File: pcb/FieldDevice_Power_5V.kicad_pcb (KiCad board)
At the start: 2 copper layers, 25 parts, among them J1 Itp_1, J2 V in 6-18V, J3 Itp_2, J4 V out 5V, J5 Vtp_2, J6 Vtp_1, J7 Battery, U1 TPS54232

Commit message: More on the layout
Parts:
- BT1: moved to B.Cu
- D1: value D_Schottky -> B130-13-F
- D2: value D_Schottky -> B130-13-F; footprint Diodes_SMD:D_SOD-123F -> FieldDevice_Power_5V:B130-13-F
- D3: footprint Diodes_SMD:D_SOD-123F -> FieldDevice_Power_5V:D_SOD-123F
- J1, J2, J3, J4, J5, J6: footprint Pin_Headers:Pin_Header_Straight_1x02_Pitch2.54mm -> Pin_Headers:Pin_Header_Angled_1x02_Pitch2.54mm
- J7: footprint Pin_Headers:Pin_Header_Straight_1x01 -> Pin_Headers:Pin_Header_Angled_1x01
- moved J5 98.1 mm to (70.9, 48.5), turned to 90 degrees
- moved D2 94.9 mm to (74.4, 80.1), turned to 270 degrees
- moved D1 94.1 mm to (75.9, 74.9)
- moved C4 90.4 mm to (84.1, 61.7), turned to 270 degrees
- moved J1 88.9 mm to (66.0, 73.4), turned to 180 degrees
- moved C2 88.5 mm to (80.0, 68.7), turned to 90 degrees
- moved J3 88.3 mm to (77.2, 48.5), turned to 90 degrees
- moved C3 86.4 mm to (84.2, 68.6), turned to 90 degrees
- moved R1 85.2 mm to (89.4, 77.0)
- moved C7 77.8 mm to (93.0, 75.4)
- moved L1 75.0 mm to (95.2, 57.4), turned to 180 degrees
- moved C1 72.4 mm to (108.0, 66.8)
- moved R4 72.3 mm to (101.3, 74.4)
- moved U1 72.0 mm to (94.2, 69.8)
- moved BT1 71.8 mm to (90.2, 50.8)
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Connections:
- J6 pad 1: /VIN -> GND
- J6 pad 2: GND -> /VIN
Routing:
- net /Vout: track 0.00 -> 79.2 mm
- net /V+: track 0.00 -> 14.0 mm
- net /VSENSE: track 0.00 -> 13.4 mm
- net /BATT: track 0.00 -> 12.9 mm, vias 0 -> 1
- net /COMP: track 0.00 -> 6.49 mm
- net GND: track 0.00 -> 6.30 mm
- net Net-(C6-Pad1): track 0.00 -> 2.43 mm
- added copper zone on F.Cu, net /PH
- added copper zone on F.Cu, net /VIN
- added copper zone on F.Cu, net /Vout
- added copper zone on B.Cu, net GND
- added copper zone on F.Cu, net GND
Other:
- net class Default: clearance 0.2 -> 0.254; trace_width 0.25 -> 0.254; via_dia 0.6 -> 0.381; via_drill 0.4 -> 0.254
- rule pad_to_mask_clearance: 0.2 -> 0
- rule trace_clearance: 0.2 -> 0.254
- rule trace_min: 0.2 -> 0.254
- rule via_min_drill: 0.3 -> 0.254
- rule via_min_size: 0.4 -> 0.381

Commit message: Finishing up the layout
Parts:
- added ST**: STITCH_VIA, FieldDevice_Power_5V:STITCH_VIA, F.Cu at (95.8, 77.2)
- added ST**: STITCH_VIA, FieldDevice_Power_5V:STITCH_VIA, F.Cu at (94.7, 73.4)
- added ST**: STITCH_VIA, FieldDevice_Power_5V:STITCH_VIA, F.Cu at (93.2, 81.0)
- added ST**: STITCH_VIA, FieldDevice_Power_5V:STITCH_VIA, F.Cu at (90.7, 81.0)
- added ST**: STITCH_VIA, FieldDevice_Power_5V:STITCH_VIA, F.Cu at (88.1, 81.0)
- added ST**: STITCH_VIA, FieldDevice_Power_5V:STITCH_VIA, F.Cu at (85.6, 81.0)
- added ST**: STITCH_VIA, FieldDevice_Power_5V:STITCH_VIA, F.Cu at (83.1, 81.0)
- added ST**: STITCH_VIA, FieldDevice_Power_5V:STITCH_VIA, F.Cu at (80.5, 81.0)
- added ST**: STITCH_VIA, FieldDevice_Power_5V:STITCH_VIA, F.Cu at (78.0, 81.0)
- added ST**: STITCH_VIA, FieldDevice_Power_5V:STITCH_VIA, F.Cu at (72.9, 81.0)
- added ST**: STITCH_VIA, FieldDevice_Power_5V:STITCH_VIA, F.Cu at (70.4, 81.0)
- added ST**: STITCH_VIA, FieldDevice_Power_5V:STITCH_VIA, F.Cu at (67.8, 81.0)
- added ST**: STITCH_VIA, FieldDevice_Power_5V:STITCH_VIA, F.Cu at (94.7, 72.1)
- added ST**: STITCH_VIA, FieldDevice_Power_5V:STITCH_VIA, F.Cu at (65.3, 81.0)
- added ST**: STITCH_VIA, FieldDevice_Power_5V:STITCH_VIA, F.Cu at (88.1, 67.3)
- added ST**: STITCH_VIA, FieldDevice_Power_5V:STITCH_VIA, F.Cu at (78.0, 67.3)
- added ST**: STITCH_VIA, FieldDevice_Power_5V:STITCH_VIA, F.Cu at (75.4, 67.3)
- added ST**: STITCH_VIA, FieldDevice_Power_5V:STITCH_VIA, F.Cu at (70.4, 67.3)
- added ST**: STITCH_VIA, FieldDevice_Power_5V:STITCH_VIA, F.Cu at (65.3, 67.3)
- added ST**: STITCH_VIA, FieldDevice_Power_5V:STITCH_VIA, F.Cu at (88.1, 64.8)
- added ST**: STITCH_VIA, FieldDevice_Power_5V:STITCH_VIA, F.Cu at (85.6, 64.8)
- added ST**: STITCH_VIA, FieldDevice_Power_5V:STITCH_VIA, F.Cu at (83.1, 64.8)
- added ST**: STITCH_VIA, FieldDevice_Power_5V:STITCH_VIA, F.Cu at (80.5, 64.8)
- added ST**: STITCH_VIA, FieldDevice_Power_5V:STITCH_VIA, F.Cu at (94.7, 70.9)
- added ST**: STITCH_VIA, FieldDevice_Power_5V:STITCH_VIA, F.Cu at (78.0, 64.8)
- added ST**: STITCH_VIA, FieldDevice_Power_5V:STITCH_VIA, F.Cu at (75.4, 64.8)
- added ST**: STITCH_VIA, FieldDevice_Power_5V:STITCH_VIA, F.Cu at (72.9, 64.8)
- added ST**: STITCH_VIA, FieldDevice_Power_5V:STITCH_VIA, F.Cu at (70.4, 64.8)
- added ST**: STITCH_VIA, FieldDevice_Power_5V:STITCH_VIA, F.Cu at (65.3, 64.8)
- added ST**: STITCH_VIA, FieldDevice_Power_5V:STITCH_VIA, F.Cu at (93.2, 62.2)
- added ST**: STITCH_VIA, FieldDevice_Power_5V:STITCH_VIA, F.Cu at (90.7, 62.2)
- added ST**: STITCH_VIA, FieldDevice_Power_5V:STITCH_VIA, F.Cu at (88.1, 62.2)
- added ST**: STITCH_VIA, FieldDevice_Power_5V:STITCH_VIA, F.Cu at (85.6, 62.2)
- added ST**: STITCH_VIA, FieldDevice_Power_5V:STITCH_VIA, F.Cu at (83.1, 62.2)
- added ST**: STITCH_VIA, FieldDevice_Power_5V:STITCH_VIA, F.Cu at (94.7, 69.6)
- added ST**: STITCH_VIA, FieldDevice_Power_5V:STITCH_VIA, F.Cu at (80.5, 62.2)
- added ST**: STITCH_VIA, FieldDevice_Power_5V:STITCH_VIA, F.Cu at (78.0, 62.2)
- added ST**: STITCH_VIA, FieldDevice_Power_5V:STITCH_VIA, F.Cu at (75.4, 62.2)
- added ST**: STITCH_VIA, FieldDevice_Power_5V:STITCH_VIA, F.Cu at (72.9, 62.2)
- added ST**: STITCH_VIA, FieldDevice_Power_5V:STITCH_VIA, F.Cu at (70.4, 62.2)
- added ST**: STITCH_VIA, FieldDevice_Power_5V:STITCH_VIA, F.Cu at (67.8, 62.2)
- added ST**: STITCH_VIA, FieldDevice_Power_5V:STITCH_VIA, F.Cu at (65.3, 62.2)
- added ST**: STITCH_VIA, FieldDevice_Power_5V:STITCH_VIA, F.Cu at (93.7, 73.4)
- added ST**: STITCH_VIA, FieldDevice_Power_5V:STITCH_VIA, F.Cu at (93.7, 72.1)
- added ST**: STITCH_VIA, FieldDevice_Power_5V:STITCH_VIA, F.Cu at (93.7, 70.9)
- added ST**: STITCH_VIA, FieldDevice_Power_5V:STITCH_VIA, F.Cu at (93.7, 69.6)
- added ST**: STITCH_VIA, FieldDevice_Power_5V:STITCH_VIA, F.Cu at (94.7, 68.3)
- added ST**: STITCH_VIA, FieldDevice_Power_5V:STITCH_VIA, F.Cu at (93.7, 68.3)
- added ST**: STITCH_VIA, FieldDevice_Power_5V:STITCH_VIA, F.Cu at (94.7, 78.5)
- added ST**: STITCH_VIA, FieldDevice_Power_5V:STITCH_VIA, F.Cu at (113.5, 91.2)
- added ST**: STITCH_VIA, FieldDevice_Power_5V:STITCH_VIA, F.Cu at (111.0, 91.2)
- added ST**: STITCH_VIA, FieldDevice_Power_5V:STITCH_VIA, F.Cu at (108.5, 91.2)
- added ST**: STITCH_VIA, FieldDevice_Power_5V:STITCH_VIA, F.Cu at (105.9, 91.2)
- added ST**: STITCH_VIA, FieldDevice_Power_5V:STITCH_VIA, F.Cu at (103.4, 91.2)
- added ST**: STITCH_VIA, FieldDevice_Power_5V:STITCH_VIA, F.Cu at (100.8, 91.2)
- added ST**: STITCH_VIA, FieldDevice_Power_5V:STITCH_VIA, F.Cu at (98.3, 91.2)
- added ST**: STITCH_VIA, FieldDevice_Power_5V:STITCH_VIA, F.Cu at (95.8, 91.2)
- added ST**: STITCH_VIA, FieldDevice_Power_5V:STITCH_VIA, F.Cu at (93.2, 91.2)
- added ST**: STITCH_VIA, FieldDevice_Power_5V:STITCH_VIA, F.Cu at (90.7, 91.2)
- added ST**: STITCH_VIA, FieldDevice_Power_5V:STITCH_VIA, F.Cu at (96.8, 78.5)
- added ST**: STITCH_VIA, FieldDevice_Power_5V:STITCH_VIA, F.Cu at (88.1, 91.2)
- added ST**: STITCH_VIA, FieldDevice_Power_5V:STITCH_VIA, F.Cu at (85.6, 91.2)
- added ST**: STITCH_VIA, FieldDevice_Power_5V:STITCH_VIA, F.Cu at (83.1, 91.2)
- added ST**: STITCH_VIA, FieldDevice_Power_5V:STITCH_VIA, F.Cu at (80.5, 91.2)
- added ST**: STITCH_VIA, FieldDevice_Power_5V:STITCH_VIA, F.Cu at (78.0, 91.2)
- added ST**: STITCH_VIA, FieldDevice_Power_5V:STITCH_VIA, F.Cu at (75.4, 91.2)
- added ST**: STITCH_VIA, FieldDevice_Power_5V:STITCH_VIA, F.Cu at (72.9, 91.2)
- added ST**: STITCH_VIA, FieldDevice_Power_5V:STITCH_VIA, F.Cu at (70.4, 91.2)
- added ST**: STITCH_VIA, FieldDevice_Power_5V:STITCH_VIA, F.Cu at (67.8, 91.2)
- added ST**: STITCH_VIA, FieldDevice_Power_5V:STITCH_VIA, F.Cu at (65.3, 91.2)
- added ST**: STITCH_VIA, FieldDevice_Power_5V:STITCH_VIA, F.Cu at (96.8, 75.9)
- added ST**: STITCH_VIA, FieldDevice_Power_5V:STITCH_VIA, F.Cu at (113.5, 88.6)
- added ST**: STITCH_VIA, FieldDevice_Power_5V:STITCH_VIA, F.Cu at (111.0, 88.6)
- added ST**: STITCH_VIA, FieldDevice_Power_5V:STITCH_VIA, F.Cu at (108.5, 88.6)
- added ST**: STITCH_VIA, FieldDevice_Power_5V:STITCH_VIA, F.Cu at (105.9, 88.6)
- added ST**: STITCH_VIA, FieldDevice_Power_5V:STITCH_VIA, F.Cu at (103.4, 88.6)
- added ST**: STITCH_VIA, FieldDevice_Power_5V:STITCH_VIA, F.Cu at (100.8, 88.6)
- added ST**: STITCH_VIA, FieldDevice_Power_5V:STITCH_VIA, F.Cu at (98.3, 88.6)
- added ST**: STITCH_VIA, FieldDevice_Power_5V:STITCH_VIA, F.Cu at (95.8, 88.6)
- added ST**: STITCH_VIA, FieldDevice_Power_5V:STITCH_VIA, F.Cu at (93.2, 88.6)
- added ST**: STITCH_VIA, FieldDevice_Power_5V:STITCH_VIA, F.Cu at (90.7, 88.6)
- added ST**: STITCH_VIA, FieldDevice_Power_5V:STITCH_VIA, F.Cu at (94.7, 75.9)
- added ST**: STITCH_VIA, FieldDevice_Power_5V:STITCH_VIA, F.Cu at (88.1, 88.6)
- added ST**: STITCH_VIA, FieldDevice_Power_5V:STITCH_VIA, F.Cu at (85.6, 88.6)
- added ST**: STITCH_VIA, FieldDevice_Power_5V:STITCH_VIA, F.Cu at (83.1, 88.6)
- added ST**: STITCH_VIA, FieldDevice_Power_5V:STITCH_VIA, F.Cu at (80.5, 88.6)
- added ST**: STITCH_VIA, FieldDevice_Power_5V:STITCH_VIA, F.Cu at (78.0, 88.6)
- added ST**: STITCH_VIA, FieldDevice_Power_5V:STITCH_VIA, F.Cu at (75.4, 88.6)
- added ST**: STITCH_VIA, FieldDevice_Power_5V:STITCH_VIA, F.Cu at (72.9, 88.6)
- added ST**: STITCH_VIA, FieldDevice_Power_5V:STITCH_VIA, F.Cu at (70.4, 88.6)
- added ST**: STITCH_VIA, FieldDevice_Power_5V:STITCH_VIA, F.Cu at (65.3, 88.6)
- added ST**: STITCH_VIA, FieldDevice_Power_5V:STITCH_VIA, F.Cu at (113.5, 86.1)
- added ST**: STITCH_VIA, FieldDevice_Power_5V:STITCH_VIA, F.Cu at (94.7, 67.1)
- added ST**: STITCH_VIA, FieldDevice_Power_5V:STITCH_VIA, F.Cu at (111.0, 86.1)
- added ST**: STITCH_VIA, FieldDevice_Power_5V:STITCH_VIA, F.Cu at (108.5, 86.1)
- added ST**: STITCH_VIA, FieldDevice_Power_5V:STITCH_VIA, F.Cu at (105.9, 86.1)
- added ST**: STITCH_VIA, FieldDevice_Power_5V:STITCH_VIA, F.Cu at (103.4, 86.1)
- added ST**: STITCH_VIA, FieldDevice_Power_5V:STITCH_VIA, F.Cu at (100.8, 86.1)
- added ST**: STITCH_VIA, FieldDevice_Power_5V:STITCH_VIA, F.Cu at (98.3, 86.1)
- added ST**: STITCH_VIA, FieldDevice_Power_5V:STITCH_VIA, F.Cu at (95.8, 86.1)
- added ST**: STITCH_VIA, FieldDevice_Power_5V:STITCH_VIA, F.Cu at (93.2, 86.1)
- added ST**: STITCH_VIA, FieldDevice_Power_5V:STITCH_VIA, F.Cu at (85.6, 86.1)
- added ST**: STITCH_VIA, FieldDevice_Power_5V:STITCH_VIA, F.Cu at (83.1, 86.1)
- added ST**: STITCH_VIA, FieldDevice_Power_5V:STITCH_VIA, F.Cu at (93.7, 67.1)
- added ST**: STITCH_VIA, FieldDevice_Power_5V:STITCH_VIA, F.Cu at (80.5, 86.1)
- added ST**: STITCH_VIA, FieldDevice_Power_5V:STITCH_VIA, F.Cu at (78.0, 86.1)
- added ST**: STITCH_VIA, FieldDevice_Power_5V:STITCH_VIA, F.Cu at (75.4, 86.1)
- added ST**: STITCH_VIA, FieldDevice_Power_5V:STITCH_VIA, F.Cu at (65.3, 86.1)
- added ST**: STITCH_VIA, FieldDevice_Power_5V:STITCH_VIA, F.Cu at (113.5, 83.6)
- added ST**: STITCH_VIA, FieldDevice_Power_5V:STITCH_VIA, F.Cu at (111.0, 83.6)
- added ST**: STITCH_VIA, FieldDevice_Power_5V:STITCH_VIA, F.Cu at (108.5, 83.6)
- added ST**: STITCH_VIA, FieldDevice_Power_5V:STITCH_VIA, F.Cu at (105.9, 83.6)
- added ST**: STITCH_VIA, FieldDevice_Power_5V:STITCH_VIA, F.Cu at (103.4, 83.6)
- added ST**: STITCH_VIA, FieldDevice_Power_5V:STITCH_VIA, F.Cu at (100.8, 83.6)
- added ST**: STITCH_VIA, FieldDevice_Power_5V:STITCH_VIA, F.Cu at (96.8, 73.4)
- added ST**: STITCH_VIA, FieldDevice_Power_5V:STITCH_VIA, F.Cu at (98.3, 83.6)
- added ST**: STITCH_VIA, FieldDevice_Power_5V:STITCH_VIA, F.Cu at (95.8, 83.6)
- added ST**: STITCH_VIA, FieldDevice_Power_5V:STITCH_VIA, F.Cu at (93.2, 83.6)
- added ST**: STITCH_VIA, FieldDevice_Power_5V:STITCH_VIA, F.Cu at (88.1, 83.6)
- added ST**: STITCH_VIA, FieldDevice_Power_5V:STITCH_VIA, F.Cu at (85.6, 83.6)
- added ST**: STITCH_VIA, FieldDevice_Power_5V:STITCH_VIA, F.Cu at (83.1, 83.6)
- added ST**: STITCH_VIA, FieldDevice_Power_5V:STITCH_VIA, F.Cu at (80.5, 83.6)
- added ST**: STITCH_VIA, FieldDevice_Power_5V:STITCH_VIA, F.Cu at (78.0, 83.6)
- added ST**: STITCH_VIA, FieldDevice_Power_5V:STITCH_VIA, F.Cu at (75.4, 83.6)
- added ST**: STITCH_VIA, FieldDevice_Power_5V:STITCH_VIA, F.Cu at (72.9, 83.6)
- added ST**: STITCH_VIA, FieldDevice_Power_5V:STITCH_VIA, F.Cu at (95.8, 73.4)
- added ST**: STITCH_VIA, FieldDevice_Power_5V:STITCH_VIA, F.Cu at (70.4, 83.6)
- added ST**: STITCH_VIA, FieldDevice_Power_5V:STITCH_VIA, F.Cu at (67.8, 83.6)
- added ST**: STITCH_VIA, FieldDevice_Power_5V:STITCH_VIA, F.Cu at (65.3, 83.6)
- added ST**: STITCH_VIA, FieldDevice_Power_5V:STITCH_VIA, F.Cu at (113.5, 81.0)
- added ST**: STITCH_VIA, FieldDevice_Power_5V:STITCH_VIA, F.Cu at (111.0, 81.0)
- added ST**: STITCH_VIA, FieldDevice_Power_5V:STITCH_VIA, F.Cu at (108.5, 81.0)
- added ST**: STITCH_VIA, FieldDevice_Power_5V:STITCH_VIA, F.Cu at (105.9, 81.0)
- added ST**: STITCH_VIA, FieldDevice_Power_5V:STITCH_VIA, F.Cu at (103.4, 81.0)
- added ST**: STITCH_VIA, FieldDevice_Power_5V:STITCH_VIA, F.Cu at (98.3, 81.0)
- added ST**: STITCH_VIA, FieldDevice_Power_5V:STITCH_VIA, F.Cu at (95.8, 81.0)
- J1, J3, J5, J6: footprint Pin_Headers:Pin_Header_Angled_1x02_Pitch2.54mm -> Pin_Headers:Pin_Header_Straight_1x02_Pitch2.54mm
- J7: footprint Pin_Headers:Pin_Header_Angled_1x01 -> FieldDevice_Power_5V:Pin_Header_Angled_1x01
- moved J2 7.58 mm to (68.1, 66.0)
- moved J7 6.67 mm to (68.1, 89.4)
- moved J1 1.78 mm to (66.0, 71.6), turned to 0 degrees
- moved C1 1.02 mm to (108.0, 67.8)
- moved C2 0.78 mm to (80.8, 68.6)
- moved J4 0.25 mm to (83.6, 48.3)
- moved C3 0.16 mm to (84.3, 68.6)
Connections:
- net Net-(J3-Pad2) renamed /V5+
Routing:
- net /BOOT: track 0.00 -> 28.8 mm, vias 0 -> 2
- net Net-(D1-Pad2): track 0.00 -> 14.4 mm, vias 0 -> 1
- net /EN: track 0.00 -> 10.6 mm
- net /V5+: track 0.00 -> 3.92 mm
- net /SS: track 0.00 -> 3.82 mm
- net /VIN: track 0.00 -> 2.79 mm
- net /V+: track 14.0 -> 14.2 mm, vias 0 -> 1
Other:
- board outline added: 51.6 x 48 mm

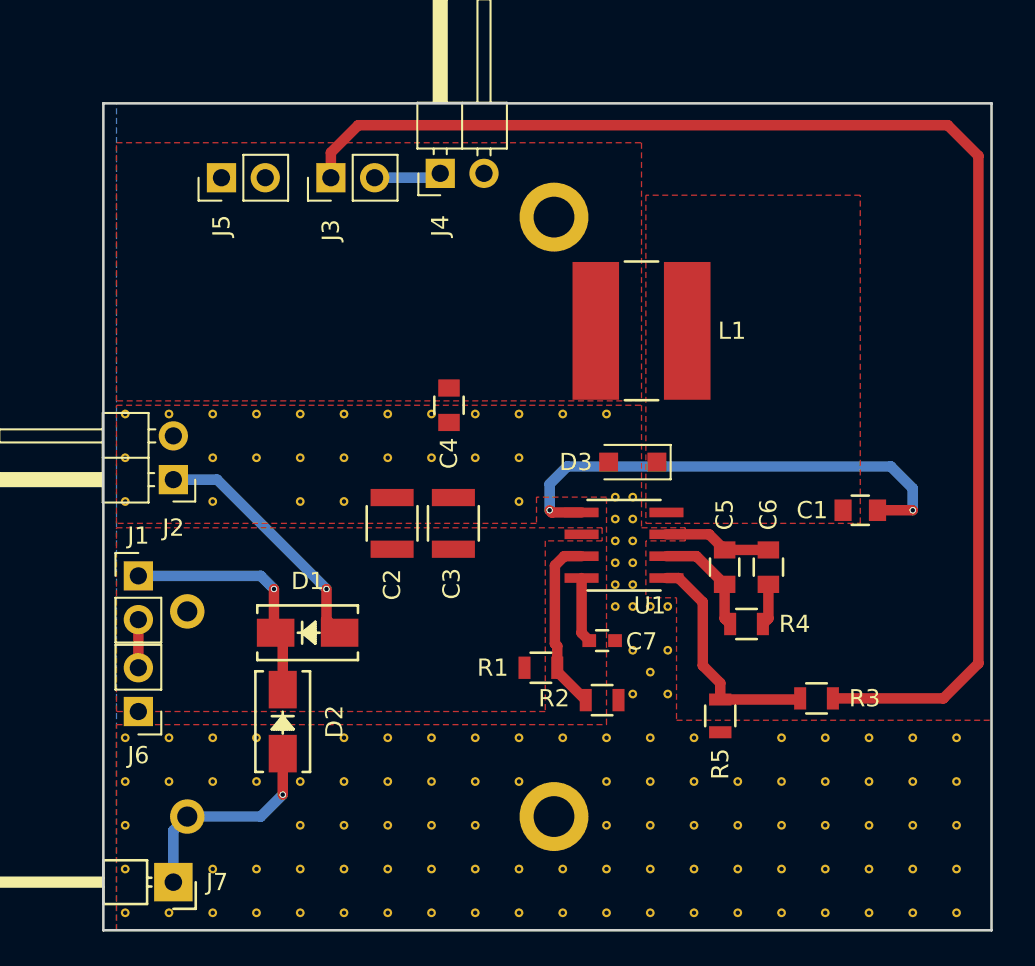
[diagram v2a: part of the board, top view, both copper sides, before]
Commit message: Finalised the layout and prepared Gerbers
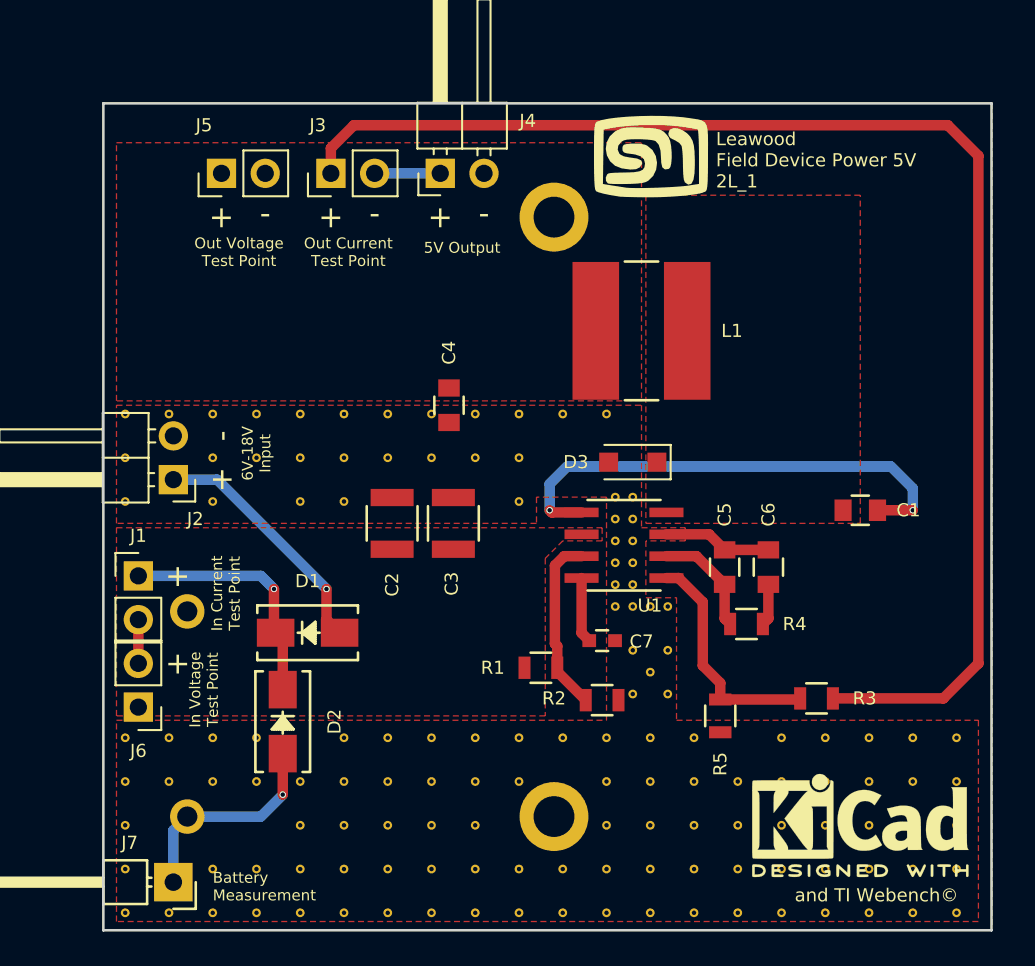
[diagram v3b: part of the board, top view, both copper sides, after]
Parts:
- added G***: LOGO, FieldDevice_Power_5V:MyBasic_rounded_50_1, F.Cu at (95.8, 47.2)
- added REF***: KiCad-Logo2_6mm_SilkScreen, Symbols:KiCad-Logo2_6mm_SilkScreen, F.Cu at (108.0, 86.1)
- moved J3 0.25 mm to (77.2, 48.3)
- moved J5 0.25 mm to (70.9, 48.3)
- moved J6 0.25 mm to (66.0, 79.2)
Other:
- board text added: "+"
- board text added: "-"
- board text added: "5V Output"
- board text added: "6V-18V Input"
- board text added: "Battery Measurement"
- board text added: "In Current Test Point"
- board text added: "In Voltage Test Point"
- board text added: "Leawood Field Device Power 5V 2L_1"
- board text added: "Out Current Test Point"
- board text added: "Out Voltage Test Point"
- board text added: "and TI Webench©"

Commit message: Fixed up some nomenclature
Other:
- board text added: "*"
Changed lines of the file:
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@@
     (area 57.142999 37.430999 120.430191 93.8631)
     (thickness 1.6)
-    (drawings 23)
+    (drawings 24)
     (tracks 68)
     (zones 0)
@@
   )
   (setup
-    (last_trace_width 0.6096)
+    (last_trace_width 0.254)
     (user_trace_width 0.3048)
     (user_trace_width 0.6096)
@@
     (pad_to_mask_clearance 0)
     (aux_axis_origin 0 0)
-    (visible_elements FFFEFF7F)
+    (visible_elements 7FFEEF7F)
     (pcbplotparams
       (layerselection 0x010f8_80000001)
@@
       (drillshape 0)
       (scaleselection 1)
-      (outputdirectory gerbers/))
+      (outputdirectory ../doc/))
   )
   (net 0 "")
@@
     (tags "capacitor 0805")
     (attr smd)
-    (fp_text reference C1 (at 2.794 0) (layer F.SilkS)
+    (fp_text reference C1 (at -0.05 1.682) (layer F.SilkS)
       (effects (font (size 0.762 0.762) (thickness 0.127)))
     )
@@
     (tags "capacitor 1210")
     (attr smd)
-    (fp_text reference C2 (at -3.556 0 90) (layer F.SilkS)
+    (fp_text reference C2 (at 0.08 -2.372 90) (layer F.SilkS)
       (effects (font (size 0.762 0.762) (thickness 0.127)))
     )
@@
     (tags "capacitor 1210")
     (attr smd)
-    (fp_text reference C3 (at -3.5052 -0.1016 90) (layer F.SilkS)
+    (fp_text reference C3 (at -0.02 2.472 90) (layer F.SilkS)
       (effects (font (size 0.762 0.762) (thickness 0.127)))
     )
@@
     (tags "capacitor 0805")
     (attr smd)
-    (fp_text reference C4 (at -3.048 0 270) (layer F.SilkS)
+    (fp_text reference C4 (at -0.022 -1.726 270) (layer F.SilkS)
       (effects (font (size 0.762 0.762) (thickness 0.127)))
     )
@@
     (tags "capacitor 0805")
     (attr smd)
-    (fp_text reference C5 (at 3.048 0 90) (layer F.SilkS)
+    (fp_text reference C5 (at -0.08 -1.576 90) (layer F.SilkS)
       (effects (font (size 0.762 0.762) (thickness 0.127)))
     )
@@
     (tags "capacitor 0805")
     (attr smd)
-    (fp_text reference C6 (at 3.048 0 90) (layer F.SilkS)
+    (fp_text reference C6 (at 0.02 1.684 90) (layer F.SilkS)
       (effects (font (size 0.762 0.762) (thickness 0.127)))
     )
@@
     (tags "capacitor 0603")
     (attr smd)
-    (fp_text reference C7 (at 2.286 0.0508) (layer F.SilkS)
+    (fp_text reference C7 (at 0.036 -1.2872) (layer F.SilkS)
       (effects (font (size 0.762 0.762) (thickness 0.127)))
     )
@@
     (descr "Through hole angled pin header, 1x02, 2.54mm pitch, 6mm pin length, single row")
     (tags "Through hole angled pin header THT 1x02 2.54mm single row")
-    (fp_text reference J2 (at -1.27 -2.286 180) (layer F.SilkS)
+    (fp_text reference J2 (at 2.372 4.94 180) (layer F.SilkS)
       (effects (font (size 0.762 0.762) (thickness 0.127)))
     )
@@
     (tags "resistor 0805")
     (attr smd)
-    (fp_text reference R1 (at -2.794 0) (layer F.SilkS)
+    (fp_text reference R1 (at -0.008 -1.662) (layer F.SilkS)
       (effects (font (size 0.762 0.762) (thickness 0.127)))
     )
@@
     (tags "resistor 0805")
     (attr smd)
-    (fp_text reference R2 (at -2.794 -0.1016) (layer F.SilkS)
+    (fp_text reference R2 (at 0.036 1.6584) (layer F.SilkS)
       (effects (font (size 0.762 0.762) (thickness 0.127)))
     )
@@
     (tags "resistor 0805")
     (attr smd)
-    (fp_text reference R3 (at -2.794 0 180) (layer F.SilkS)
+    (fp_text reference R3 (at 0.01 1.64 180) (layer F.SilkS)
       (effects (font (size 0.762 0.762) (thickness 0.127)))
     )
@@
     (tags "resistor 0805")
     (attr smd)
-    (fp_text reference R4 (at 2.794 0) (layer F.SilkS)
+    (fp_text reference R4 (at -0.046 1.678) (layer F.SilkS)
       (effects (font (size 0.762 0.762) (thickness 0.127)))
     )
@@
     (tags "resistor 0805")
     (attr smd)
-    (fp_text reference R5 (at 2.794 0 270) (layer F.SilkS)
+    (fp_text reference R5 (at -0.056 1.622 270) (layer F.SilkS)
       (effects (font (size 0.762 0.762) (thickness 0.127)))
     )
@@
     (descr "Through hole straight pin header, 1x02, 2.54mm pitch, single row")
     (tags "Through hole pin header THT 1x02 2.54mm single row")
-    (fp_text reference J1 (at 0 -2.33) (layer F.SilkS)
+    (fp_text reference J1 (at -0.34 -2.028) (layer F.SilkS)
       (effects (font (size 0.762 0.762) (thickness 0.127)))
     )
@@
   (module FieldDevice_Power_5V:B130-13-F (layer F.Cu)
     (at 75.8668 74.93)
-    (fp_text reference D1 (at 0 -3) (layer F.SilkS)
+    (fp_text reference D1 (at 0.0332 -2.33) (layer F.SilkS)
       (effects (font (size 0.762 0.762) (thickness 0.127)))
     )
@@
   (module FieldDevice_Power_5V:B130-13-F (layer F.Cu)
     (at 74.422 80.0892 270)
-    (fp_text reference D2 (at 0 -3 270) (layer F.SilkS)
+    (fp_text reference D2 (at -0.0892 -2.378 270) (layer F.SilkS)
       (effects (font (size 0.762 0.762) (thickness 0.127)))
     )
@@
       (xy 1.195199 0.12652) (xy 1.195199 0.12652)) (layer F.SilkS) (width 0.1))
   )
+  (gr_text * (at 91.5 67.4) (layer F.SilkS)
+    (effects (font (thickness 0.127)))
+  )
   (gr_text "and TI Webench©" (at 104.14 90.17) (layer F.SilkS)
